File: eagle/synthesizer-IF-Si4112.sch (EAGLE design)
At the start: 39 parts, among them J1 142-0701-851, J3 142-0701-851, Q1 PMOS, U1 SI4112, X1 ECS-TXO-3225

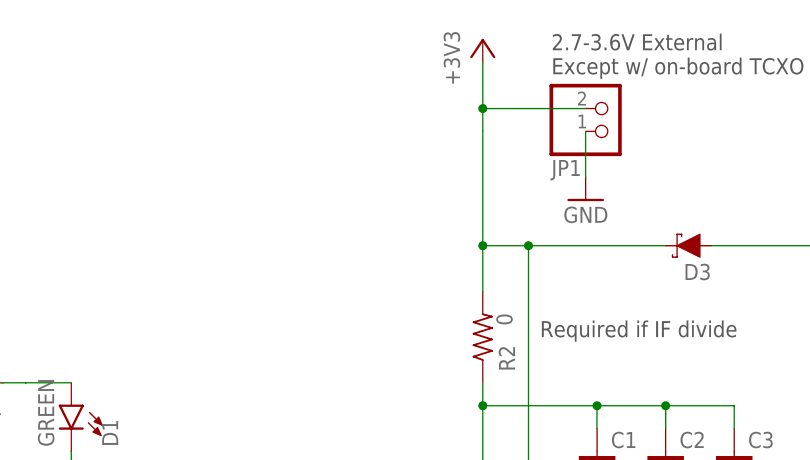
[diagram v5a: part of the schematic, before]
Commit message: Si4112 add 1u cap
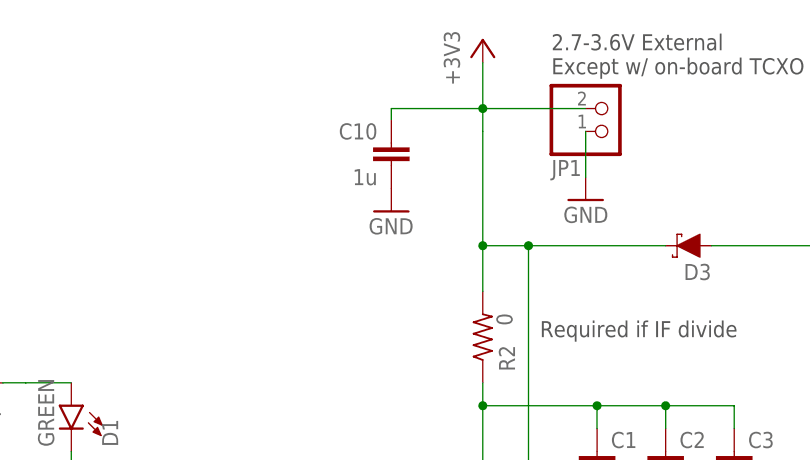
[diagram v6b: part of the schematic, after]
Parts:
- added C10: 1u, oresat-rcl:C-EU0603-B-NOSILK
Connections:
- net +3V3: now also C10.1
- net GND: now also C10.2
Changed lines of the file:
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@@
 <part name="R3" library="oresat-rcl" deviceset="R-US_" device="0402-B-NOSILK" value="47k"/>
 <part name="GND16" library="supply1" deviceset="GND" device=""/>
+<part name="C10" library="oresat-rcl" deviceset="C-EU" device="0603-B-NOSILK" value="1u"/>
+<part name="GND17" library="supply1" library_urn="urn:adsk.eagle:library:371" deviceset="GND" device=""/>
 </parts>
 <sheets>
@@
 <attribute name="VALUE" x="76.2" y="115.57" size="1.778" layer="96"/>
 </instance>
+<instance part="C10" gate="CE" x="139.7" y="179.07" smashed="yes" rot="MR0">
+<attribute name="NAME" x="138.176" y="179.451" size="1.778" layer="95" rot="MR0"/>
+<attribute name="VALUE" x="138.176" y="174.371" size="1.778" layer="96" rot="MR0"/>
+</instance>
+<instance part="GND17" gate="1" x="139.7" y="171.45" smashed="yes">
+<attribute name="VALUE" x="137.16" y="168.91" size="1.778" layer="96"/>
+</instance>
 </instances>
 <busses>
@@
 <pinref part="R3" gate="R" pin="1"/>
 <pinref part="GND16" gate="1" pin="GND"/>
+</segment>
+<segment>
+<pinref part="GND17" gate="1" pin="GND"/>
+<pinref part="C10" gate="CE" pin="2"/>
 </segment>
 </net>
@@
 <wire x1="154.94" y1="167.64" x2="170.18" y2="167.64" width="0.1524" layer="91"/>
 <junction x="154.94" y="167.64"/>
-</segment>
-<segment>
+<pinref part="C10" gate="CE" pin="1"/>
+<wire x1="139.7" y1="181.61" x2="139.7" y2="182.88" width="0.1524" layer="91"/>
+<wire x1="139.7" y1="182.88" x2="149.86" y2="182.88" width="0.1524" layer="91"/>
+</segment>
+<segment>

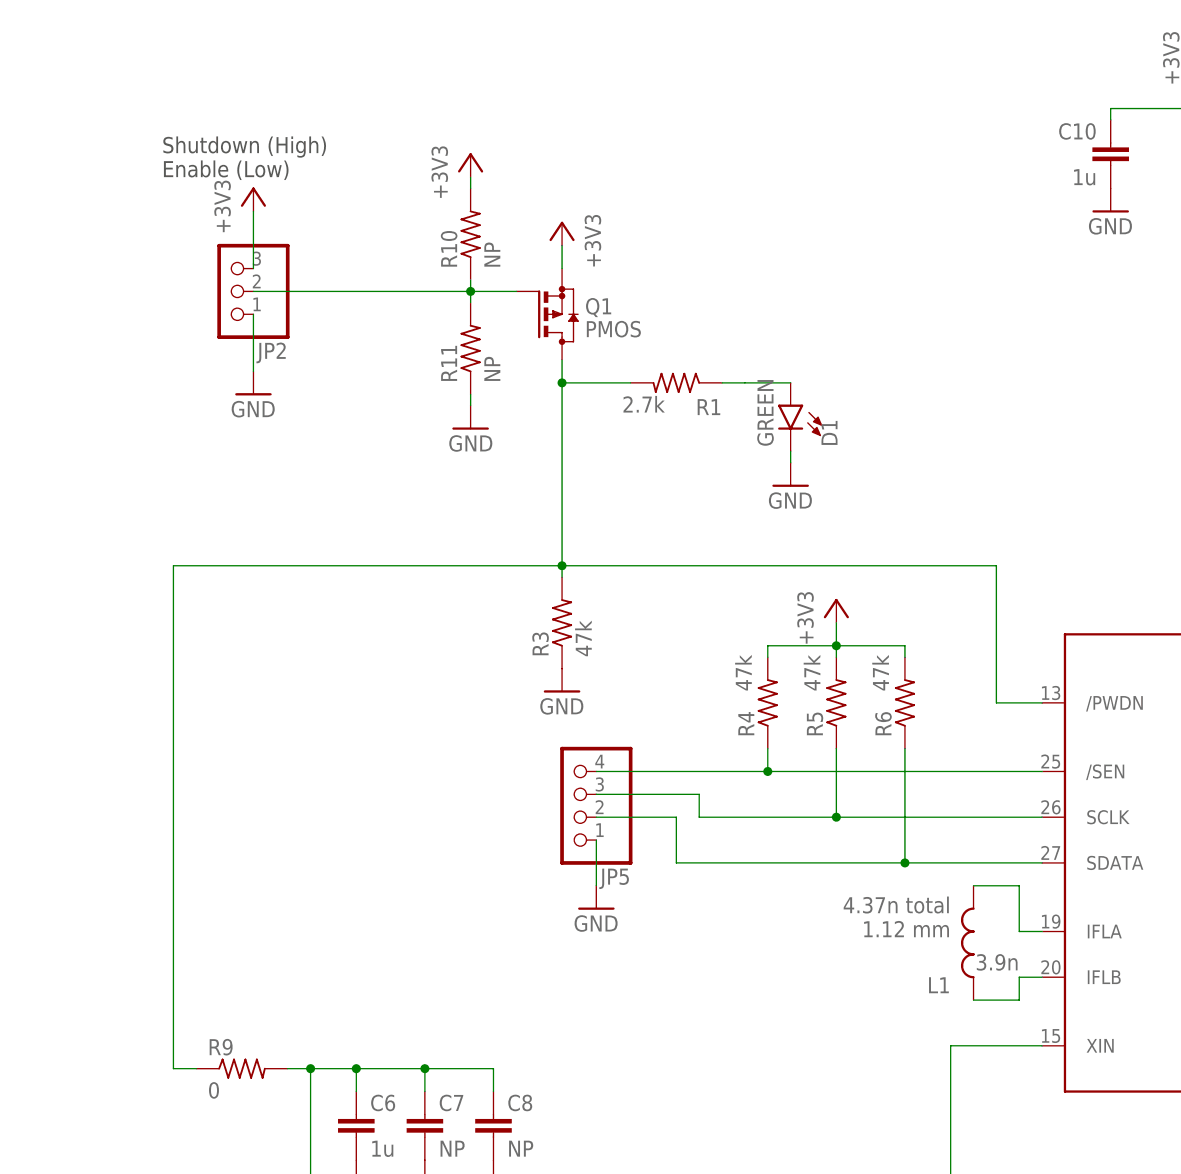
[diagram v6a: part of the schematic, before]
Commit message: Synth LO Si4112, notes
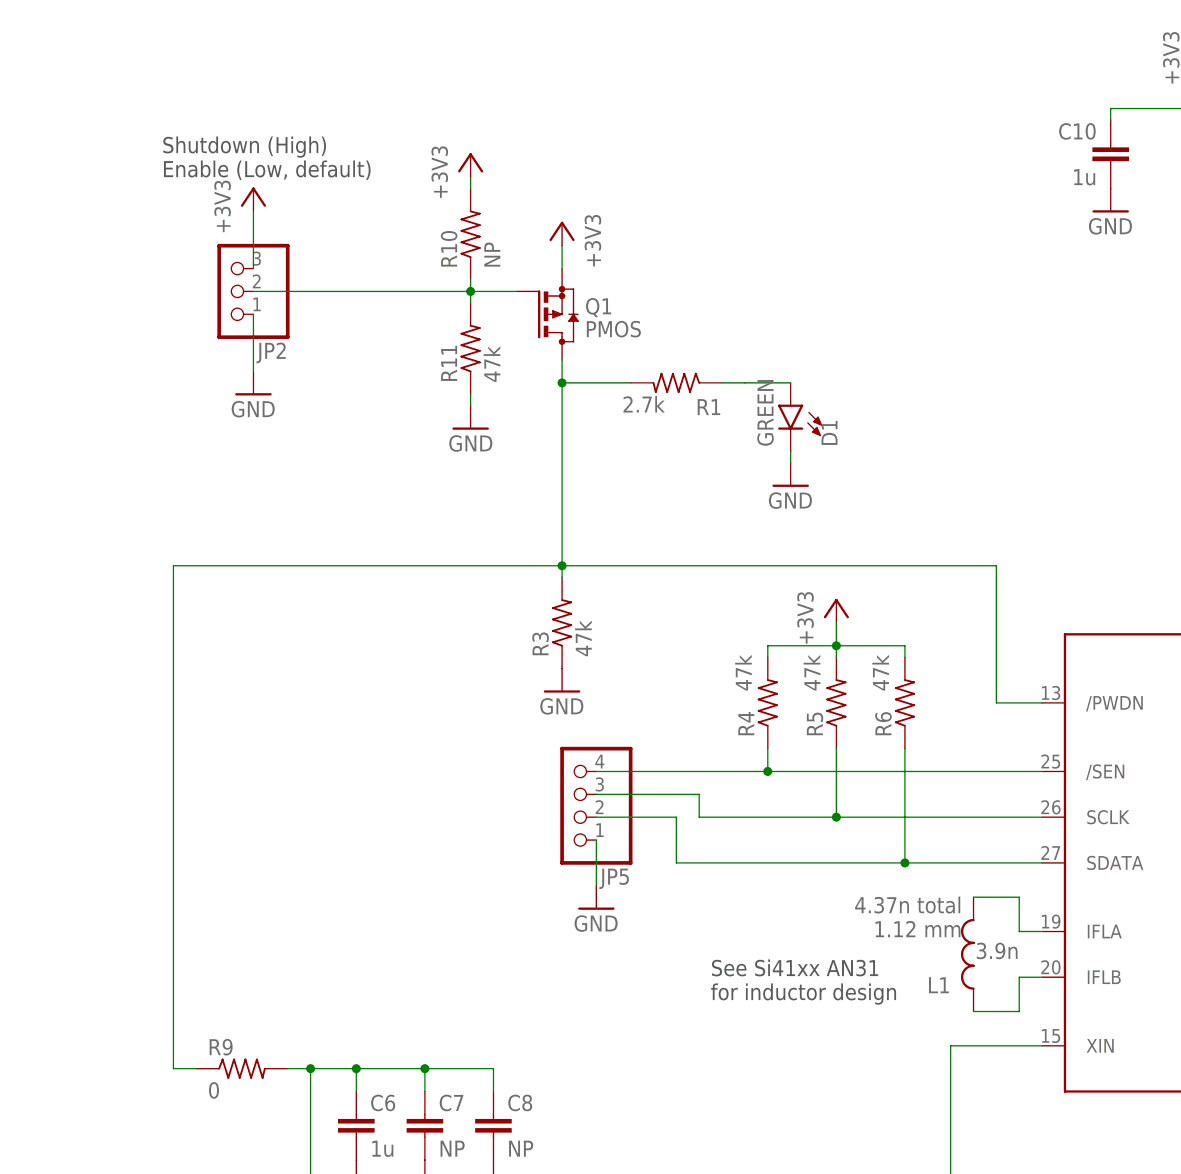
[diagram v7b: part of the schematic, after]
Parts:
- R11: value NP -> 47k
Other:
- note added: "See Si41xx AN31 for inductor design"
- note added: "Shutdown (High) Enable (Low, default)"
- note removed: "Shutdown (High) Enable (Low)"
- moved on the sheet: L1
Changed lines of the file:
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@@
 <part name="GND13" library="supply1" library_urn="urn:adsk.eagle:library:371" deviceset="GND" device=""/>
 <part name="X1" library="X-ECS-TXO-TCXO" deviceset="ECS-TXO-3225" device=""/>
-<part name="R11" library="oresat-rcl" deviceset="R-US_" device="0402-B-NOSILK" value="NP"/>
+<part name="R11" library="oresat-rcl" deviceset="R-US_" device="0402-B-NOSILK" value="47k"/>
 <part name="GND69" library="supply1" library_urn="urn:adsk.eagle:library:371" deviceset="GND" device=""/>
 <part name="C2" library="oresat-rcl" deviceset="C-EU" device="0603-B-NOSILK" value="NP"/>
@@
 <text x="176.53" y="26.67" size="5.08" layer="94">IF Synthesizer for L band LO</text>
 <text x="266.7" y="6.35" size="3.81" layer="94">1</text>
-<text x="121.92" y="95.25" size="1.778" layer="96" rot="R180">4.37n total
+<text x="123.19" y="95.25" size="1.778" layer="96" rot="R180">4.37n total
 1.12 mm</text>
 <text x="156.21" y="157.48" size="1.778" layer="97">Required if IF divide</text>
@@
 Cap only required if not CMOS levels</text>
 <text x="34.29" y="175.26" size="1.778" layer="97">Shutdown (High)
-Enable (Low)</text>
+Enable (Low, default)</text>
 <text x="17.78" y="49.53" size="1.778" layer="97">TCXO VCTRL
 +/- 5ppm min
@@
 - PLL not locked</text>
 <text x="187.96" y="171.45" size="1.778" layer="97">3V Button Cell</text>
+<text x="95.25" y="83.82" size="1.778" layer="97">See Si41xx AN31
+for inductor design</text>
 </plain>
 <instances>
@@
 <attribute name="VALUE" x="44.704" y="37.211" size="1.778" layer="96"/>
 </instance>
-<instance part="L1" gate="L" x="124.46" y="91.44" smashed="yes" rot="R90">
+<instance part="L1" gate="L" x="124.46" y="90.17" smashed="yes" rot="R90">
 <attribute name="NAME" x="121.92" y="86.36" size="1.778" layer="95" rot="R180"/>
-<attribute name="VALUE" x="129.54" y="88.9" size="1.778" layer="96" rot="R180"/>
+<attribute name="VALUE" x="129.54" y="90.17" size="1.778" layer="96" rot="R180"/>
 </instance>
 <instance part="L2" gate="L" x="182.88" y="104.14" smashed="yes">
@@
 <segment>
 <pinref part="L1" gate="L" pin="2"/>
-<wire x1="124.46" y1="96.52" x2="129.54" y2="96.52" width="0.1524" layer="91"/>
-<wire x1="129.54" y1="96.52" x2="129.54" y2="91.44" width="0.1524" layer="91"/>
+<wire x1="124.46" y1="95.25" x2="129.54" y2="95.25" width="0.1524" layer="91"/>
+<wire x1="129.54" y1="95.25" x2="129.54" y2="91.44" width="0.1524" layer="91"/>
 <wire x1="129.54" y1="91.44" x2="132.08" y2="91.44" width="0.1524" layer="91"/>
 <pinref part="U1" gate="G$1" pin="IFLA"/>
@@
 <segment>
 <pinref part="L1" gate="L" pin="1"/>
-<wire x1="124.46" y1="83.82" x2="129.54" y2="83.82" width="0.1524" layer="91"/>
-<wire x1="129.54" y1="83.82" x2="129.54" y2="86.36" width="0.1524" layer="91"/>
+<wire x1="124.46" y1="82.55" x2="129.54" y2="82.55" width="0.1524" layer="91"/>
+<wire x1="129.54" y1="82.55" x2="129.54" y2="86.36" width="0.1524" layer="91"/>
 <wire x1="129.54" y1="86.36" x2="132.08" y2="86.36" width="0.1524" layer="91"/>
 <pinref part="U1" gate="G$1" pin="IFLB"/>

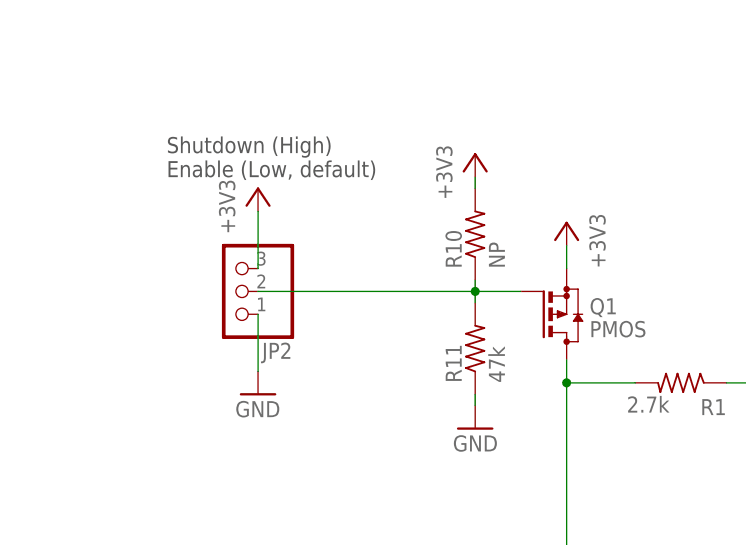
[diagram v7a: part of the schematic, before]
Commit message: Synth Si4112 change default shutdown
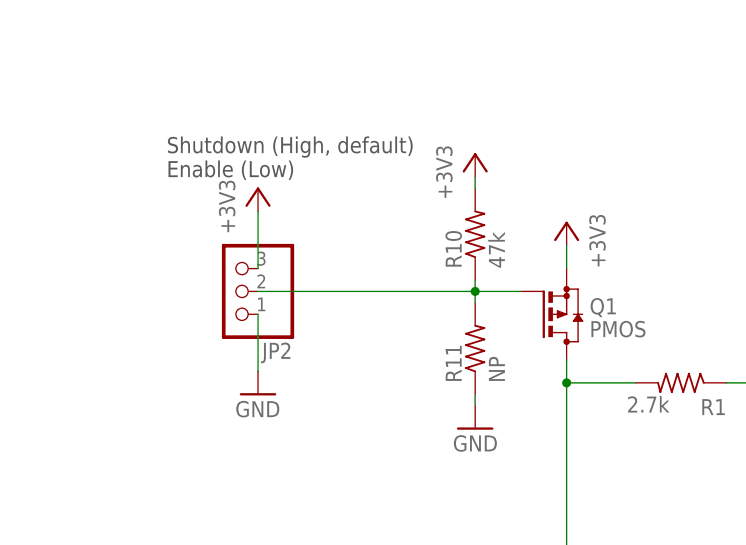
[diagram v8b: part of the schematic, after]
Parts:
- R10: value NP -> 47k
- R11: value 47k -> NP
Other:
- note added: "Shutdown (High, default) Enable (Low)"
- note removed: "Shutdown (High) Enable (Low, default)"
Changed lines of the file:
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@@
 <part name="GND13" library="supply1" library_urn="urn:adsk.eagle:library:371" deviceset="GND" device=""/>
 <part name="X1" library="X-ECS-TXO-TCXO" deviceset="ECS-TXO-3225" device=""/>
-<part name="R11" library="oresat-rcl" deviceset="R-US_" device="0402-B-NOSILK" value="47k"/>
+<part name="R11" library="oresat-rcl" deviceset="R-US_" device="0402-B-NOSILK" value="NP"/>
 <part name="GND69" library="supply1" library_urn="urn:adsk.eagle:library:371" deviceset="GND" device=""/>
 <part name="C2" library="oresat-rcl" deviceset="C-EU" device="0603-B-NOSILK" value="NP"/>
@@
 <part name="GND11" library="supply1" deviceset="GND" device=""/>
 <part name="+3V2" library="supply1" library_urn="urn:adsk.eagle:library:371" deviceset="+3V3" device=""/>
-<part name="R10" library="oresat-rcl" deviceset="R-US_" device="0402-B-NOSILK" value="NP"/>
+<part name="R10" library="oresat-rcl" deviceset="R-US_" device="0402-B-NOSILK" value="47k"/>
 <part name="+3V3" library="supply1" library_urn="urn:adsk.eagle:library:371" deviceset="+3V3" device=""/>
 <part name="JP7" library="pinhead" library_urn="urn:adsk.eagle:library:325" deviceset="PINHD-1X2" device="" package3d_urn="urn:adsk.eagle:package:22435/2"/>
@@
 <text x="101.6" y="48.26" size="1.778" layer="97">0402 Jumper
 Cap only required if not CMOS levels</text>
-<text x="34.29" y="175.26" size="1.778" layer="97">Shutdown (High)
-Enable (Low, default)</text>
+<text x="34.29" y="175.26" size="1.778" layer="97">Shutdown (High, default)
+Enable (Low)</text>
 <text x="17.78" y="49.53" size="1.778" layer="97">TCXO VCTRL
 +/- 5ppm min
